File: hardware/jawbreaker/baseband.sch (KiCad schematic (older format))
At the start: 106 parts, among them P14 XCVR_CLKOUT, P15 INTR, P16 CLKIN, P17 CLKIN_JMP, P18 OEB, P2 CLKOUT, T3 RX_BALUN, T4 TX_BALUN, U17 MAX2837, U18 MAX5864, U19 SI5351C, U26 RF LDO, X1 GSG-XTAL4PIN

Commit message: moved mixer supply from VCC to VAA
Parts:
- U17: Part Number MAX2837ETM+T -> MAX2837ETM+
- U18: Part Number MAX5864ETM+T -> MAX5864ETM+

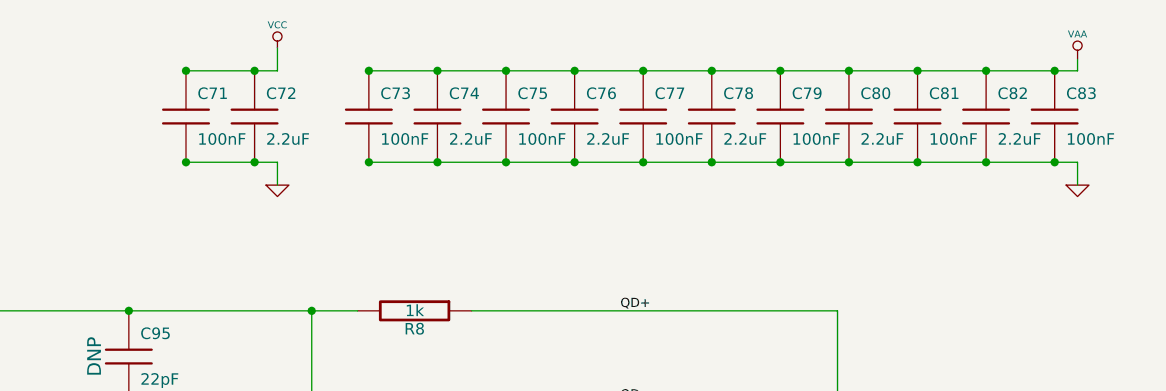
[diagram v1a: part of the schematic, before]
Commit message: moved C71 and C72 to correct supply
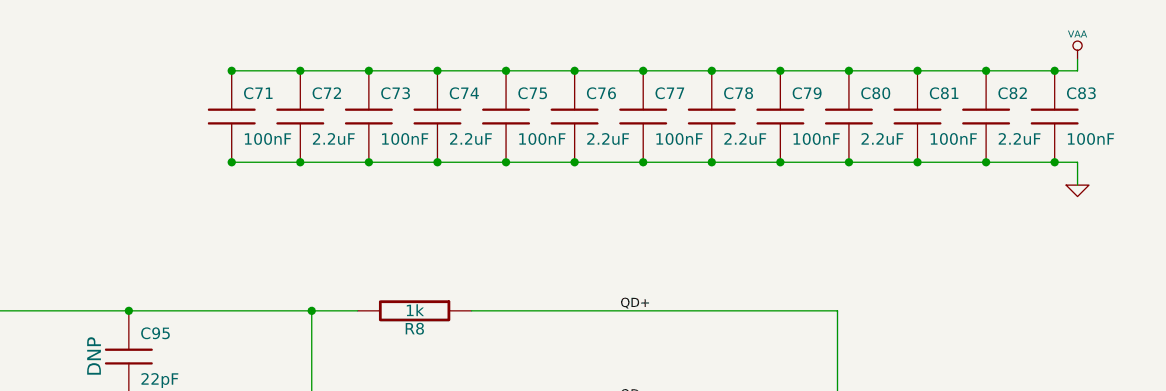
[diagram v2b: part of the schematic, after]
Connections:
- net VAA: now also C71.1, C72.1
- net VCC: no longer C71.1, C72.1
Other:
- moved on the sheet: C71, C72

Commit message: vertical through-hole SMA connectors
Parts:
- P16, P2: Description (none) -> CONN JACK SMA PCB VERT; Manufacturer (none) -> TE Connectivity; Part Number (none) -> 2081233-1
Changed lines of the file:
@@
-EESchema Schematic File Version 2  date Wed Sep  5 11:08:52 2012
+EESchema Schematic File Version 2  date Wed Sep  5 13:31:32 2012
 LIBS:power
 LIBS:device
@@
 F 0 "P2" H 5750 9750 60  0000 C CNN
 F 1 "CLKOUT" H 5750 9450 60  0000 C CNN
-F 4 "DNP" H 5500 9550 60  0000 C CNN "Note"
+F 4 "TE Connectivity" H 5750 9600 60  0001 C CNN "Manufacturer"
+F 5 "2081233-1" H 5750 9600 60  0001 C CNN "Part Number"
+F 6 "CONN JACK SMA PCB VERT" H 5750 9600 60  0001 C CNN "Description"
+F 7 "DNP" H 5500 9550 60  0000 C CNN "Note"
 	1    5750 9600
 	-1   0    0    -1
@@
 F 0 "P16" H 2700 9000 60  0000 C CNN
 F 1 "CLKIN" H 2700 8700 60  0000 C CNN
-F 4 "DNP" H 2450 8800 60  0000 C CNN "Note"
+F 4 "TE Connectivity" H 2700 8850 60  0001 C CNN "Manufacturer"
+F 5 "2081233-1" H 2700 8850 60  0001 C CNN "Part Number"
+F 6 "CONN JACK SMA PCB VERT" H 2700 8850 60  0001 C CNN "Description"
+F 7 "DNP" H 2450 8800 60  0000 C CNN "Note"
 	1    2700 8850
 	1    0    0    -1

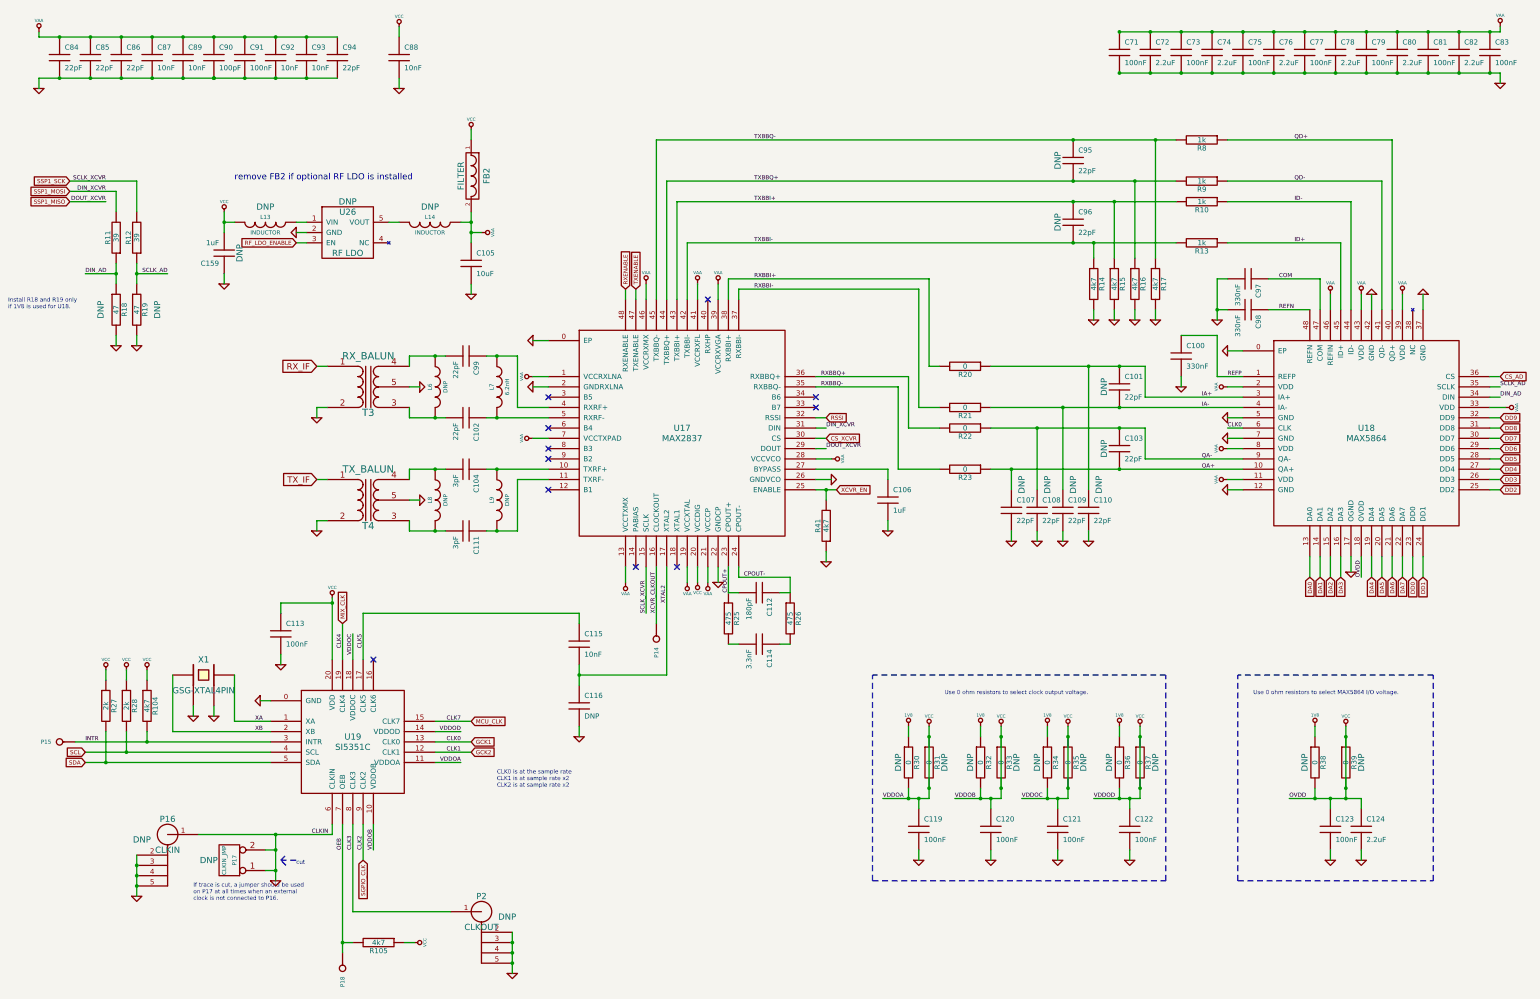
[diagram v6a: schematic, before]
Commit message: more usage of shorted resistor symbol
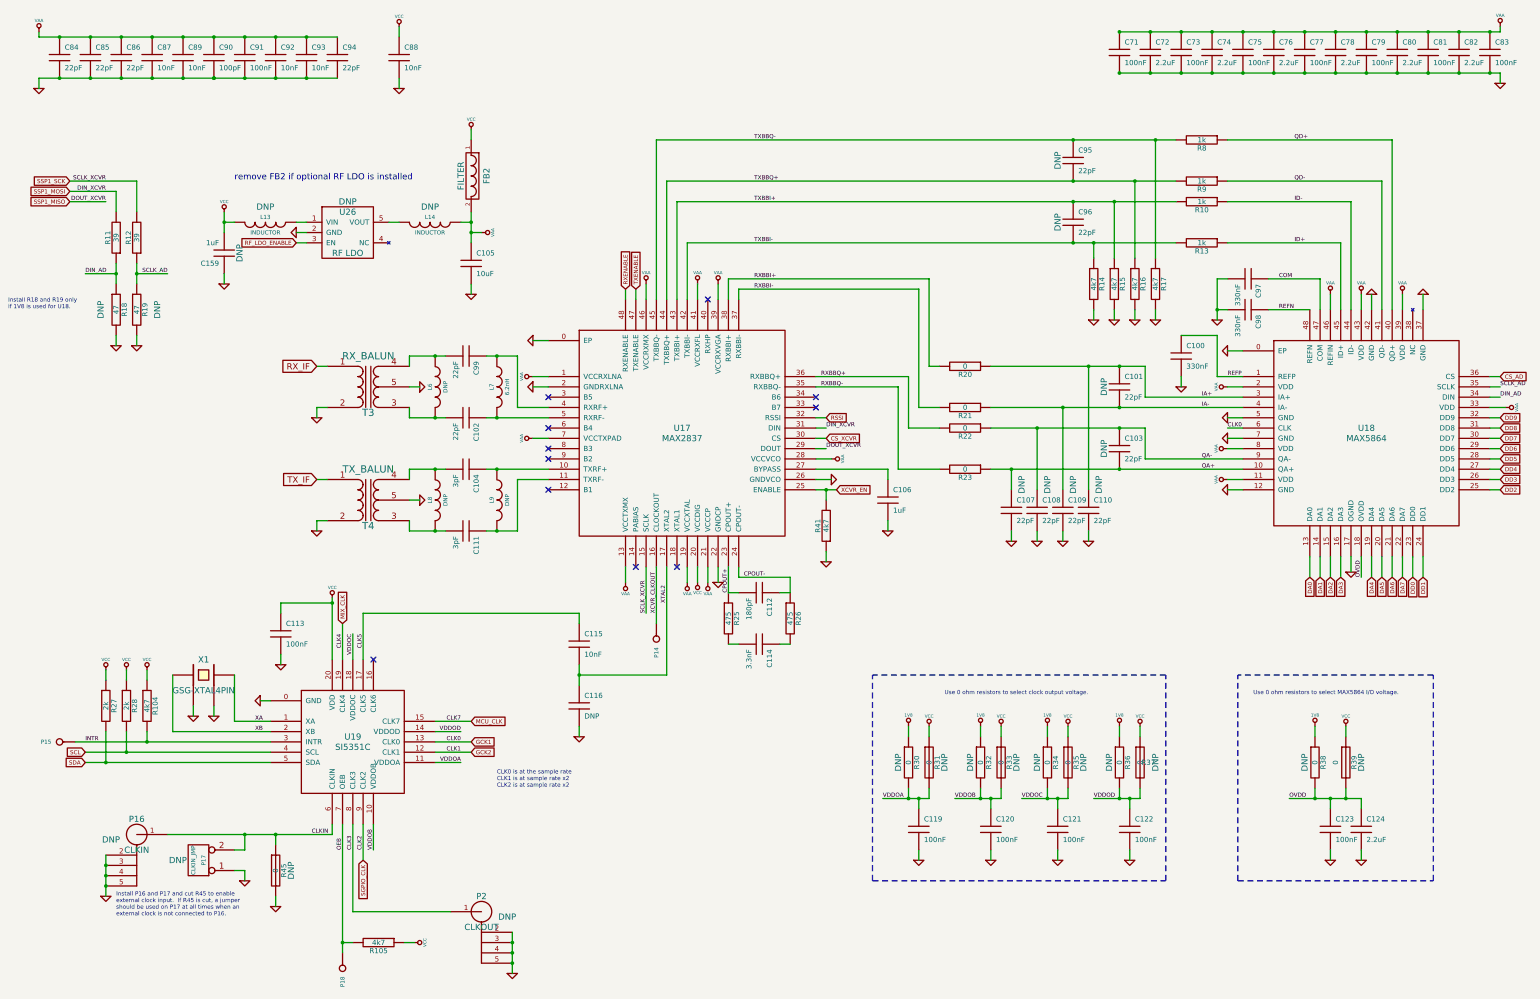
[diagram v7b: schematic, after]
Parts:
- removed R31, R33, R35, R37, R39: 0, symbol R
- added R31, R33, R35, R37, R39, R45: 0, symbol R-SHORTED
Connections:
- net GND: now also R45.2; no longer P16.1 (RF), P17.2 (PM), U19.6 (CLKIN)
- net VCC: now also R31.1, R33.1, R35.1, R37.1, R39.1; no longer C119.1, C120.1, C121.1, C122.1, C123.1, C124.1, R30.2, R32.2, R34.2, R36.2, R38.2, U18.18 (OVDD), U19.10 (VDDOB), U19.11 (VDDOA), U19.14 (VDDOD), U19.18 (VDDOC)
- new net CLKIN: P16.1 (RF), P17.2 (PM), R45.1, U19.6 (CLKIN)
- new net OVDD: C123.1, C124.1, R38.2, R39.2, U18.18 (OVDD)
- new net VDDOA: C119.1, R30.2, R31.2, U19.11 (VDDOA)
- new net VDDOB: C120.1, R32.2, R33.2, U19.10 (VDDOB)
- new net VDDOC: C121.1, R34.2, R35.2, U19.18 (VDDOC)
- new net VDDOD: C122.1, R36.2, R37.2, U19.14 (VDDOD)
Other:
- note added: "Install P16 and P17 and cut R45 to enable\nexternal clock input. If R45 is cut, a jumper\nshould be used on P17 at all times when an\nexternal clock is not connected to P16."
- note removed: "If trace is cut, a jumper should be used\non P17 at all times when an external\nclock is not connected to P16."
- note removed: "cut"
- moved on the sheet: P16, P17

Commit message: RF LDO fixes
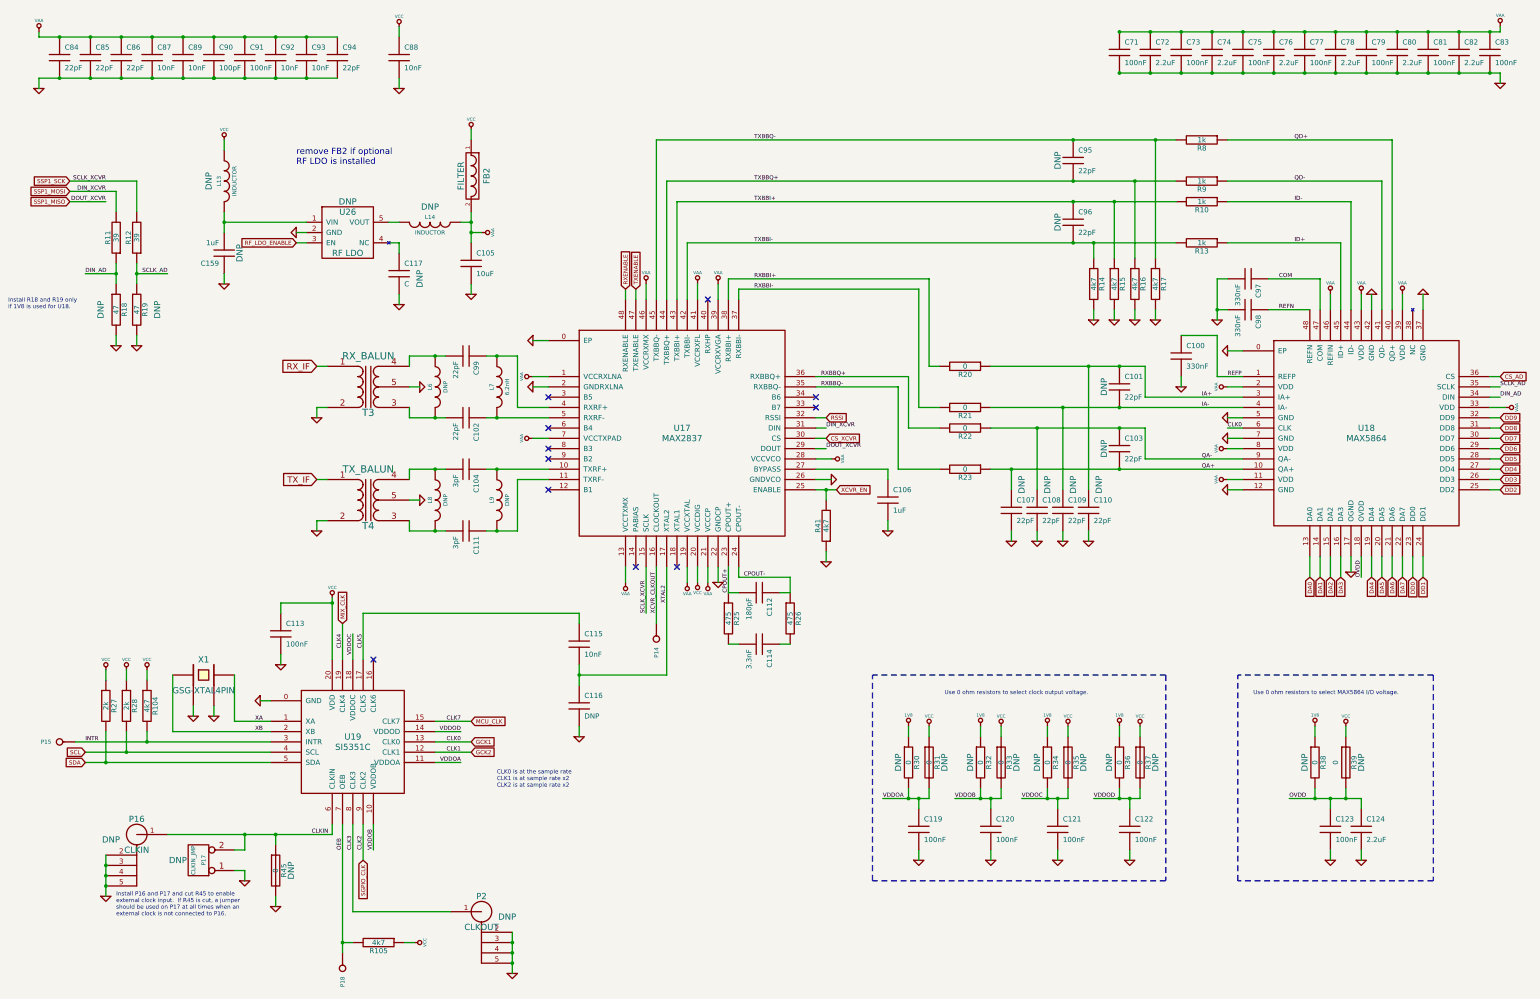
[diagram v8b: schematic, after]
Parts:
- added C117: C, symbol C
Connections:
- net GND: now also C117.2
- net VCC: now also L13.1; no longer C159.2, L13.2
- net at U26.1 (VIN): now also C159.2, L13.2; no longer L13.1
- net at U26.4 (NC): now also C117.1
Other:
- note added: "remove FB2 if optional\nRF LDO is installed"
- note removed: "remove FB2 if optional RF LDO is installed"
- moved on the sheet: L13
